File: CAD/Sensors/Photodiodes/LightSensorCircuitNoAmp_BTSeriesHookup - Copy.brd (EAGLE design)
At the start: 111 x 22.7 mm, 15 parts, among them J1 62202021121, J2 FTSH-108-02-LM-D-ES

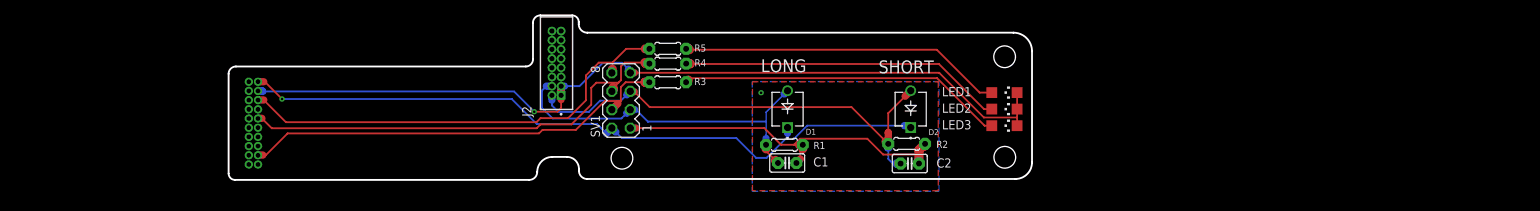
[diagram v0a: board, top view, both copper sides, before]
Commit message: restored overlay/main gpio config, added Beacon support
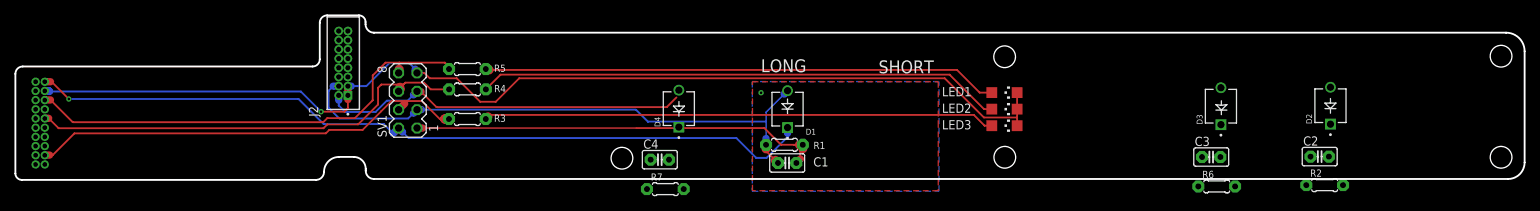
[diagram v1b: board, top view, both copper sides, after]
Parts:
- added C3, C4: (no value), adafruit:C025-025X050
- added D3, D4: BPW34S, BPW34S:DIO_BPW34S
- added R6, R7: (no value), adafruit:0204/5
- moved R2 58.0 mm to (111.8, 10.3), turned to 0 degrees
- moved D2 58.0 mm to (112.6, 21.3)
- moved C2 56.7 mm to (111.1, 14.3)
- moved J1 29.5 mm to (-65.7, 18.9)
- moved J2 29.5 mm to (-23.2, 22.7)
- moved SV1 29.5 mm to (-14.9, 22.0)
- moved R3 28.1 mm to (-6.65, 19.5)
- moved R4 27.9 mm to (-6.64, 23.6)
- moved R5 27.8 mm to (-6.65, 26.4)
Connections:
- net A: now also C3.1, C4.1, D3.A, D4.A, R6.2, R7.2
- net GND: now also C3.2, C4.2, R6.1, R7.1
- net V+: now also D3.C, D4.C
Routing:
- net GND: track 171.2 -> 209.5 mm
- net A: track 48.7 -> 78.1 mm
- net LEDR2: track 44.8 -> 72.7 mm
- net LEDR1: track 44.8 -> 71.3 mm
- net LEDR3: track 45.2 -> 70.8 mm
- net B: track 65.1 -> 51.1 mm
- net V+: track 98.8 -> 110.1 mm
- net LED1_P11: track 62.9 -> 64.6 mm
- net LED3_P12: track 61.6 -> 62.2 mm
- net LED2_P13: track 62.5 -> 62.0 mm
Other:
- board size 111 x 22.7 mm -> 208.6 x 22.7 mm
